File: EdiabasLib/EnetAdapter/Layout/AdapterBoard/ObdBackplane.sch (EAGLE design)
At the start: 11 parts

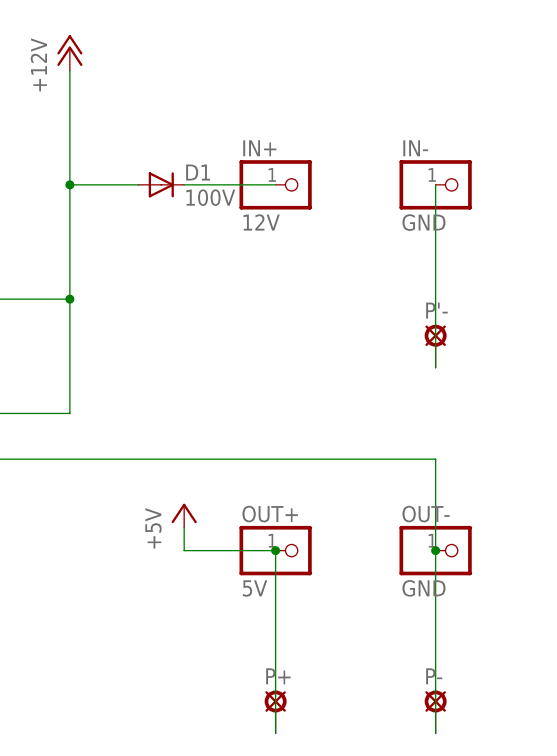
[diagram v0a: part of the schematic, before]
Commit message: Added second optional hole
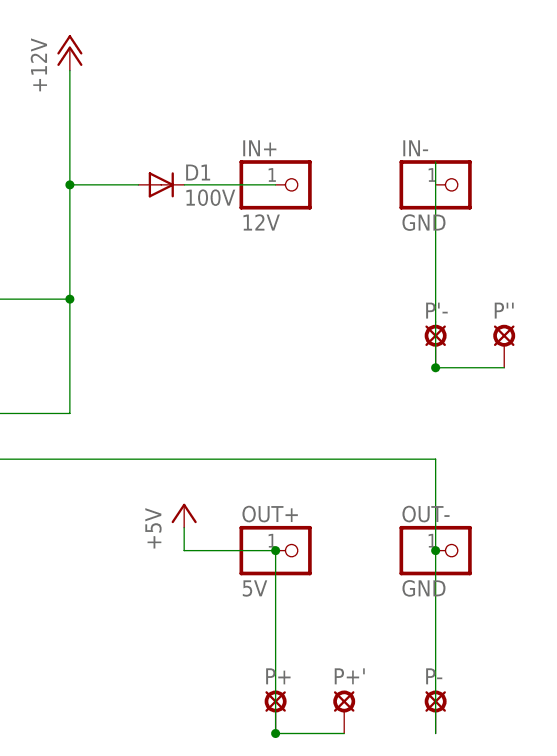
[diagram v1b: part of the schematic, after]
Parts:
- added P'', P+': SE14, solpad:SE14
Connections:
- net +5V: now also P+'.MP
- net GND2: now also P''.MP
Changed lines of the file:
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@@
 <part name="P-" library="solpad" library_urn="urn:adsk.eagle:library:364" deviceset="SE14" device="" package3d_urn="urn:adsk.eagle:package:26504/1"/>
 <part name="P'-" library="solpad" library_urn="urn:adsk.eagle:library:364" deviceset="SE14" device="" package3d_urn="urn:adsk.eagle:package:26504/1"/>
+<part name="P''" library="solpad" library_urn="urn:adsk.eagle:library:364" deviceset="SE14" device="" package3d_urn="urn:adsk.eagle:package:26504/1"/>
+<part name="P+'" library="solpad" library_urn="urn:adsk.eagle:library:364" deviceset="SE14" device="" package3d_urn="urn:adsk.eagle:package:26504/1"/>
 </parts>
 <sheets>
@@
 <instance part="P-" gate="1" x="88.9" y="152.4"/>
 <instance part="P'-" gate="1" x="88.9" y="193.04"/>
+<instance part="P''" gate="1" x="96.52" y="193.04"/>
+<instance part="P+'" gate="1" x="78.74" y="152.4"/>
 </instances>
 <busses>
@@
 <junction x="71.12" y="170.18"/>
 <pinref part="P+" gate="1" pin="MP"/>
+<pinref part="P+'" gate="1" pin="MP"/>
+<wire x1="71.12" y1="149.86" x2="78.74" y2="149.86" width="0.1524" layer="91"/>
+<junction x="71.12" y="149.86"/>
 </segment>
 </net>
@@
 <pinref part="IN-" gate="G$1" pin="1"/>
 <pinref part="P'-" gate="1" pin="MP"/>
-<wire x1="88.9" y1="210.82" x2="88.9" y2="190.5" width="0.1524" layer="91"/>
+<wire x1="88.9" y1="213.36" x2="88.9" y2="195.58" width="0.1524" layer="91"/>
+<wire x1="88.9" y1="193.04" x2="88.9" y2="190.5" width="0.1524" layer="91"/>
+<wire x1="88.9" y1="195.58" x2="88.9" y2="193.04" width="0.1524" layer="91"/>
+<pinref part="P''" gate="1" pin="MP"/>
+<wire x1="88.9" y1="190.5" x2="96.52" y2="190.5" width="0.1524" layer="91"/>
+<junction x="88.9" y="190.5"/>
 </segment>
 </net>
